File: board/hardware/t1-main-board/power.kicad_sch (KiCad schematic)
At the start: 0 parts

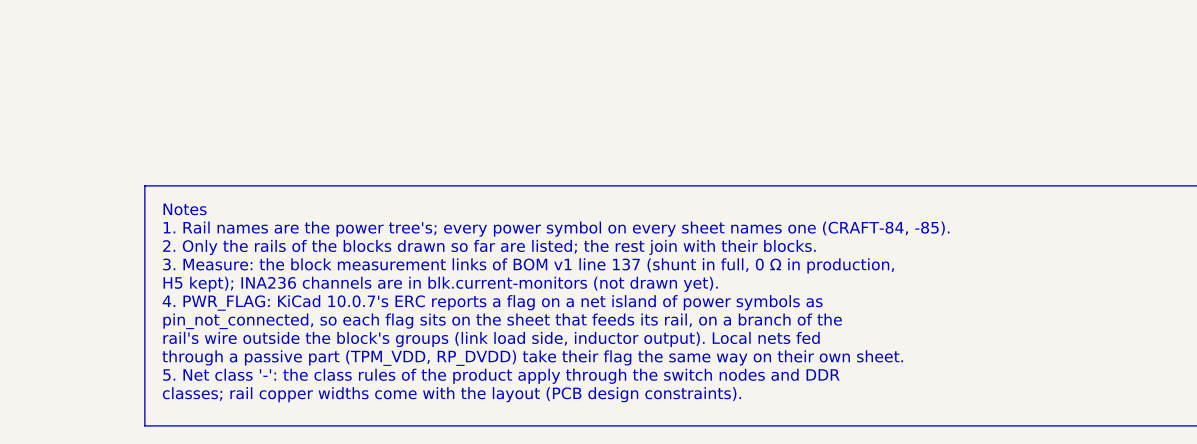
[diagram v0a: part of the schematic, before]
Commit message: Board: capture blk.current-monitors
Five INA236 on I2C1 (0x40-0x43, 0x48) with their shunts, per power tree
§4.12 and BOM v1 lines 54 and 136. The measured branches are rails of
their own (VSYS_SRC, VSYS_LV_AUDIO, VSYS_AUDIO, VSYS_LV_BL, VSYS_P5V1),
fed through the shunts on this sheet; the charger, audio, backlight and
5.1 V sheets take them. The root's layout may leave a stack level empty,
so the block sits under the notes; IC bboxes hold turned rail values;
passive rows hold a bottom rail's text.

Co-Authored-By: Claude Opus 5.5 <noreply@anthropic.com>
Claude-Session: https://claude.ai/code/session_01Ei262h3TpgY9vyfNLMi5Mn
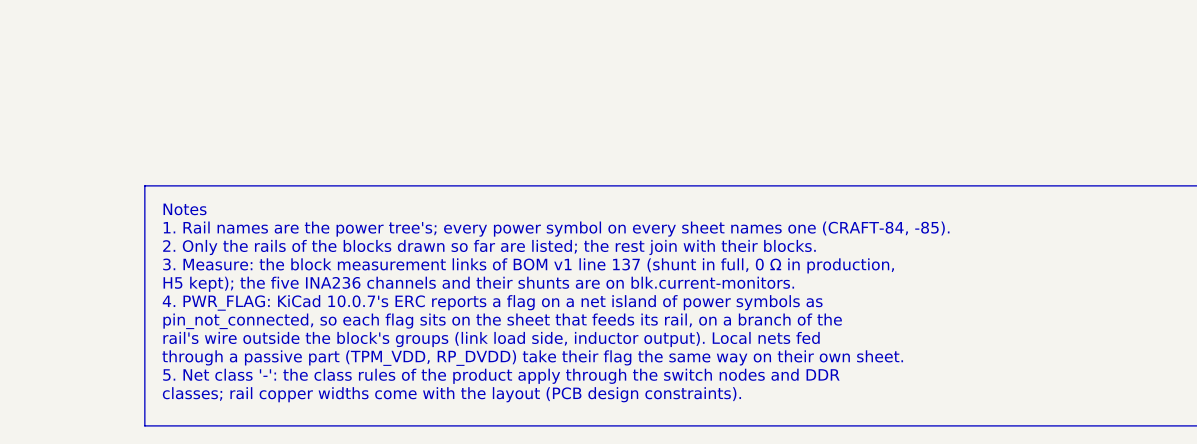
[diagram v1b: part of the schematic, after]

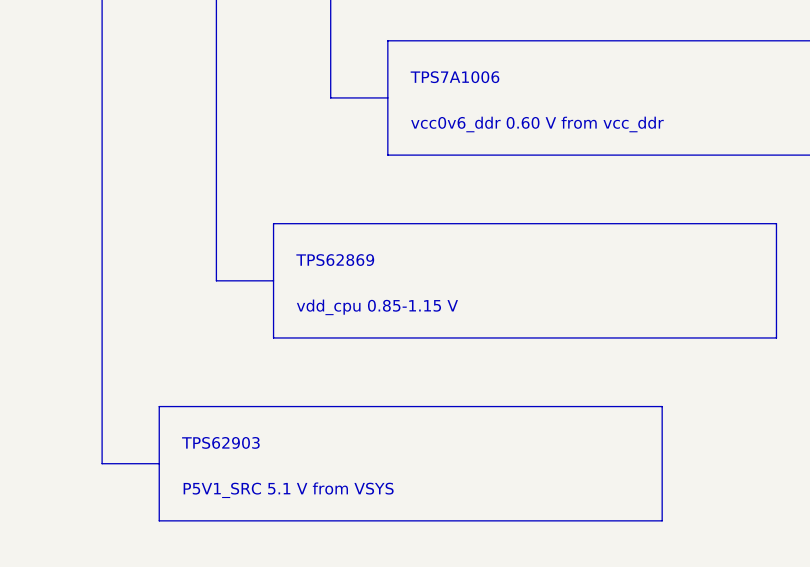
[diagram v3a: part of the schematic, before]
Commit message: vdd_cpu on the TPS62870Z4 (ADR 0026, placement v1.5)
ADR 0026 supersedes ADR 0023: TPS62870Z4WRXSR at I2C0 0x42 with the
Coilcraft XEL4012-920NE, 3 MHz, MODE/SYNC to ground with forced PWM by
register, differential sense from the 22 uF at the SoC. Output capacitance
sized at the 1.1 V devicetree cap for the 4.8 A worst-case step (peak
1.149 V, DC-bias effective values); 1800 MHz kept as a verification row.

Submodule at libs v0.3.2 (the RXS0016A land). BOM v1.18 item 8, power
tree v0.10, pinout v1 I2C0 note, feature blocks #13, placement v1.5.
Schematic regenerated, board rebuilt: 991 parts placed, 97.0 % board need,
factor 1.71, 244 capacitors within their bound, DRC 0 errors, ERC 0
errors, craft Q1 met, pcb tests pass, STEP exported (27 parts without a
model in KiCad's library, as before).

Co-Authored-By: Claude Opus 5.5 <noreply@anthropic.com>
Claude-Session: https://claude.ai/code/session_013P6pW9LdyEMFishwCcZGUr
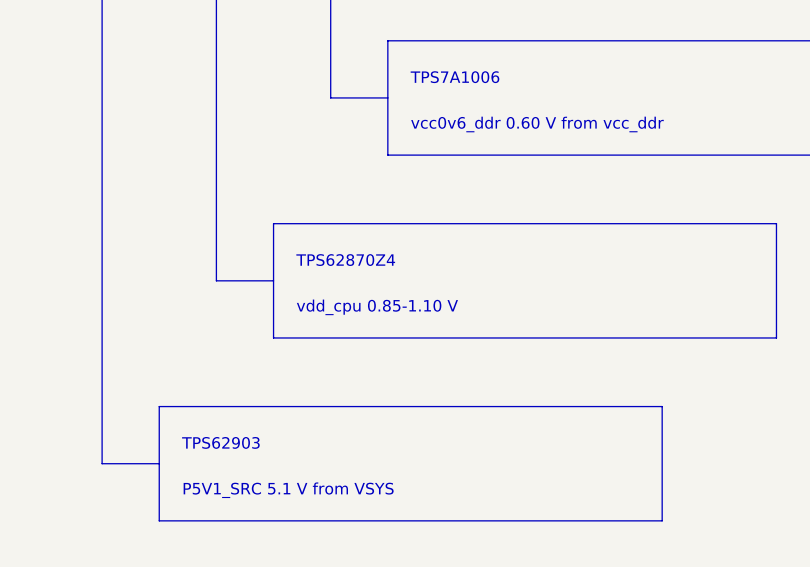
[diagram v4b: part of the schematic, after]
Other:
- note added: "TPS62870Z4"
- note added: "vdd_cpu 0.85-1.10 V"
- note removed: "TPS62869"
- note removed: "vdd_cpu 0.85-1.15 V"

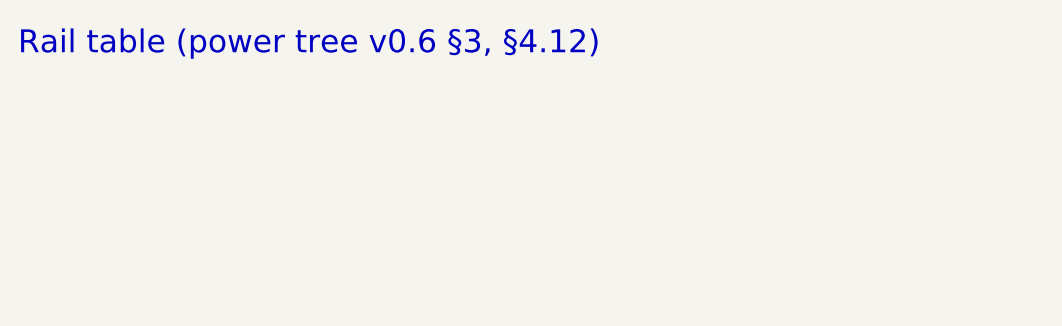
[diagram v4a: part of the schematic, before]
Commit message: Board: obsolete-audit safe fixes (BOM v1.21, power tree v0.11)
BOM quantities and owners follow the schematic (lines 34, 35, 44, 110,
121, 137); HAT input kept at 2.95 A with the DF40C-50 and the reason
recorded; power-tree HAT rows on interface v2, the PN7160 budget term
gone; SW_NODE and PCB-P-07 part lists; pinout notes; requirement,
catalog and README text; J6201; craft symmetry tables on the current
references; dead Wurth placeholder rows; stackup study inputs marked
superseded; old repository names in text and comments.

Co-Authored-By: Claude Opus 5.5 <noreply@anthropic.com>
Claude-Session: https://claude.ai/code/session_013P6pW9LdyEMFishwCcZGUr
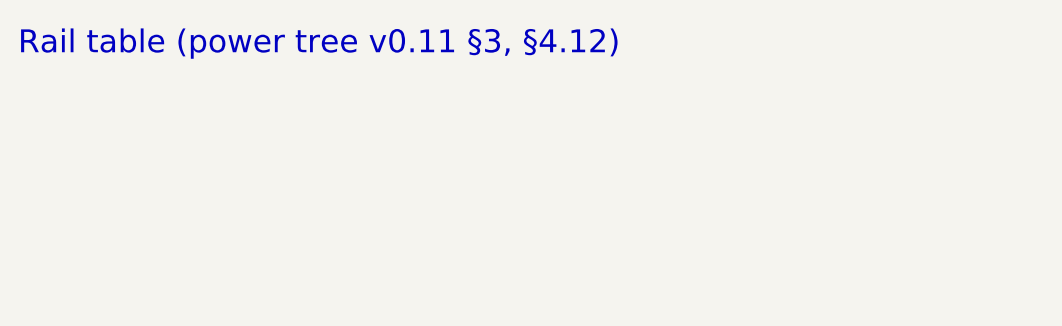
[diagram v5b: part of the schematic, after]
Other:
- note added: "Rail table (power tree v0.11 §3, §4.12)"
- note removed: "Rail table (power tree v0.6 §3, §4.12)"
